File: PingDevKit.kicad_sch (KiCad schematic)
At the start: 54 parts, among them J101 POWER, J102 DEBUG, J103 PORT1, J104 FPGA, J105 ETHERNET, J106 SYNC, J107 SONAR+, J108 SONAR+, J109 SONAR-, J110 SONAR-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

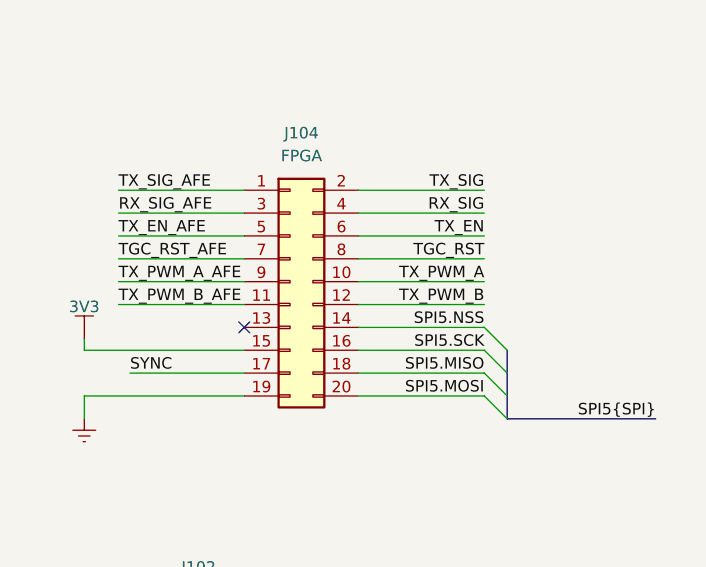
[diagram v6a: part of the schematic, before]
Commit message: new board stackup + routing
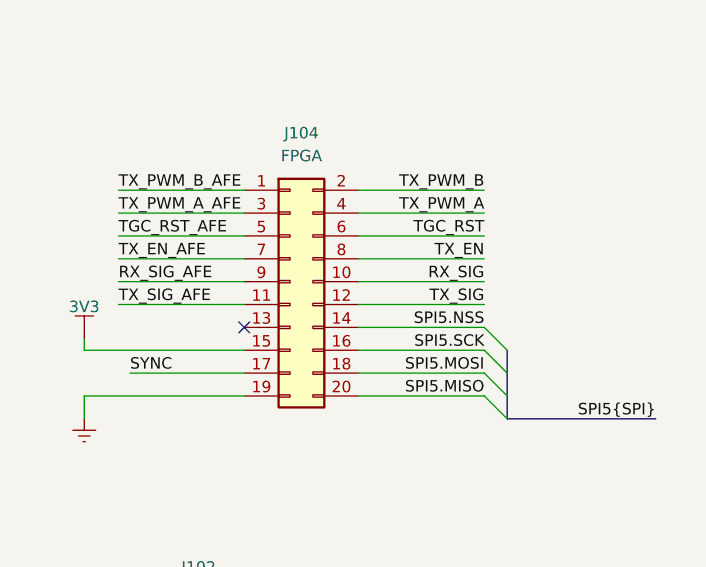
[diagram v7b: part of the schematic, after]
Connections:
- net RX_SIG: now also J104.10 (Pin_10); no longer J104.4 (Pin_4)
- net RX_SIG_AFE: now also J104.9 (Pin_9); no longer J104.3 (Pin_3)
- net SPI5.MISO: now also J104.20 (Pin_20); no longer J104.18 (Pin_18)
- net SPI5.MOSI: now also J104.18 (Pin_18); no longer J104.20 (Pin_20)
- net TGC_RST: now also J104.6 (Pin_6); no longer J104.8 (Pin_8)
- net TGC_RST_AFE: now also J104.5 (Pin_5); no longer J104.7 (Pin_7)
- net TX_EN: now also J104.8 (Pin_8); no longer J104.6 (Pin_6)
- net TX_EN_AFE: now also J104.7 (Pin_7); no longer J104.5 (Pin_5)
- net TX_PWM_A: now also J104.4 (Pin_4); no longer J104.10 (Pin_10)
- net TX_PWM_A_AFE: now also J104.3 (Pin_3); no longer J104.9 (Pin_9)
- net TX_PWM_B: now also J104.2 (Pin_2); no longer J104.12 (Pin_12)
- net TX_PWM_B_AFE: now also J104.1 (Pin_1); no longer J104.11 (Pin_11)
- net TX_SIG: now also J104.12 (Pin_12); no longer J104.2 (Pin_2)
- net TX_SIG_AFE: now also J104.11 (Pin_11); no longer J104.1 (Pin_1)
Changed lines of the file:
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@@
+		)
+	)
+	(label "TX_PWM_B_AFE"
+		(at 38.1 138.43 0)
+		(effects
+			(font
+				(size 1.27 1.27)
+			)
+			(justify left bottom)
 		)
 	)
@@
 		)
 	)
+	(label "TX_EN"
+		(at 78.74 146.05 180)
+		(effects
+			(font
+				(size 1.27 1.27)
+			)
+			(justify right bottom)
+		)
+	)
 	(label "TX_PWM_B"
 		(at 361.95 135.89 180)
@@
 		)
 	)
-	(label "TX_EN_AFE"
-		(at 38.1 143.51 0)
-		(effects
-			(font
-				(size 1.27 1.27)
-			)
-			(justify left bottom)
+	(label "TX_PWM_A"
+		(at 78.74 140.97 180)
+		(effects
+			(font
+				(size 1.27 1.27)
+			)
+			(justify right bottom)
 		)
 	)
@@
 	)
 	(label "TX_SIG"
+		(at 78.74 151.13 180)
+		(effects
+			(font
+				(size 1.27 1.27)
+			)
+			(justify right bottom)
+		)
+	)
+	(label "TX_SIG"
 		(at 269.24 129.54 0)
 		(effects
@@
 			)
 			(justify right bottom)
+		)
+	)
+	(label "TGC_RST_AFE"
+		(at 38.1 143.51 0)
+		(effects
+			(font
+				(size 1.27 1.27)
+			)
+			(justify left bottom)
 		)
 	)
@@
 		)
 	)
-	(label "TX_EN"
-		(at 78.74 143.51 180)
-		(effects
-			(font
-				(size 1.27 1.27)
-			)
-			(justify right bottom)
-		)
-	)
 	(label "VTHERM"
 		(at 269.24 134.62 0)
@@
 		)
 	)
-	(label "TX_PWM_B"
-		(at 78.74 151.13 180)
-		(effects
-			(font
-				(size 1.27 1.27)
-			)
-			(justify right bottom)
+	(label "TX_PWM_A_AFE"
+		(at 38.1 140.97 0)
+		(effects
+			(font
+				(size 1.27 1.27)
+			)
+			(justify left bottom)
 		)
 	)
@@
 			)
 			(justify right bottom)
-		)
-	)
-	(label "TX_PWM_A"
-		(at 78.74 148.59 180)
-		(effects
-			(font
-				(size 1.27 1.27)
-			)
-			(justify right bottom)
-		)
-	)
-	(label "TX_SIG_AFE"
-		(at 38.1 138.43 0)
-		(effects
-			(font
-				(size 1.27 1.27)
-			)
-			(justify left bottom)
 		)
 	)
@@
 		)
 	)
-	(label "RX_SIG"
-		(at 78.74 140.97 180)
-		(effects
-			(font
-				(size 1.27 1.27)
-			)
-			(justify right bottom)
-		)
-	)
 	(label "SPI5.SCK"
 		(at 78.74 156.21 180)
@@
 		)
 	)
-	(label "RX_SIG_AFE"
-		(at 38.1 140.97 0)
-		(effects
-			(font
-				(size 1.27 1.27)
-			)
-			(justify left bottom)
-		)
-	)
 	(label "SONAR-"
 		(at 227.33 330.2 180)
@@
 		)
 	)
-	(label "TX_SIG"
+	(label "TX_PWM_B"
 		(at 78.74 138.43 180)
 		(effects
@@
 		)
 	)
+	(label "SPI5.MISO"
+		(at 78.74 161.29 180)
+		(effects
+			(font
+				(size 1.27 1.27)
+			)
+			(justify right bottom)
+		)
+	)
 	(label "USART1.RX"
 		(at 55.88 196.85 0)
@@
 		)
 	)
+	(label "SPI5.MOSI"
+		(at 78.74 158.75 180)
+		(effects
+			(font
+				(size 1.27 1.27)
+			)
+			(justify right bottom)
+		)
+	)
 	(label "RX-"
 		(at 176.53 372.11 0)
@@
 		)
 	)
-	(label "TX_PWM_B_AFE"
-		(at 38.1 151.13 0)
-		(effects
-			(font
-				(size 1.27 1.27)
-			)
-			(justify left bottom)
-		)
-	)
 	(label "VCC_MODE"
 		(at 361.95 165.1 180)
@@
 		)
 	)
-	(label "SPI5.MISO"
-		(at 78.74 158.75 180)
-		(effects
-			(font
-				(size 1.27 1.27)
-			)
-			(justify right bottom)
-		)
-	)
 	(label "I2C1.SDA"
 		(at 396.24 109.22 180)
@@
 		)
 	)
+	(label "RX_SIG_AFE"
+		(at 38.1 148.59 0)
+		(effects
+			(font
+				(size 1.27 1.27)
+			)
+			(justify left bottom)
+		)
+	)
 	(label "PHY_nRST"
 		(at 262.89 92.71 180)
@@
 		)
 	)
-	(label "SPI5.MOSI"
-		(at 78.74 161.29 180)
-		(effects
-			(font
-				(size 1.27 1.27)
-			)
-			(justify right bottom)
-		)
-	)
-	(label "TGC_RST"
-		(at 78.74 146.05 180)
-		(effects
-			(font
-				(size 1.27 1.27)
-			)
-			(justify right bottom)
-		)
-	)
 	(label "SPI5.NSS"
 		(at 78.74 153.67 180)
@@
 		)
 	)
-	(label "TX_PWM_A_AFE"
-		(at 38.1 148.59 0)
+	(label "TX_SIG_AFE"
+		(at 38.1 151.13 0)
 		(effects
 			(font
@@
 		)
 	)
+	(label "RX_SIG"
+		(at 78.74 148.59 180)
+		(effects
+			(font
+				(size 1.27 1.27)
+			)
+			(justify right bottom)
+		)
+	)
 	(label "TX-"
 		(at 128.27 330.2 0)
@@
 		)
 	)
+	(label "TGC_RST"
+		(at 78.74 143.51 180)
+		(effects
+			(font
+				(size 1.27 1.27)
+			)
+			(justify right bottom)
+		)
+	)
 	(label "TX+"
 		(at 128.27 297.18 0)
@@
 		)
 	)
-	(label "TGC_RST_AFE"
+	(label "TX_EN_AFE"
 		(at 38.1 146.05 0)
 		(effects

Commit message: preboard review of updates
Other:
- sheet TX ports: added none; removed 3V3
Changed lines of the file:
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@@
 	(wire
 		(pts
-			(xy 167.64 196.85) (xy 167.64 207.01)
-		)
-		(stroke
-			(width 0)
-			(type default)
-		)
-	)
-	(wire
-		(pts
 			(xy 55.88 105.41) (xy 55.88 106.68)
 		)
@@
 	(wire
 		(pts
-			(xy 167.64 207.01) (xy 185.42 207.01)
-		)
-		(stroke
-			(width 0)
-			(type default)
-		)
-	)
-	(wire
-		(pts
 			(xy 227.33 54.61) (xy 238.76 54.61)
 		)
@@
 	(symbol
 		(lib_id "BR_Virtual_Parts:VCC")
-		(at 167.64 196.85 0)
-		(unit 1)
-		(exclude_from_sim no)
-		(in_bom yes)
-		(on_board yes)
-		(dnp no)
-		(property "Reference" "#PWR0154"
-			(at 167.64 200.66 0)
-			(effects
-				(font
-					(size 1.27 1.27)
-				)
-				(hide yes)
-			)
-		)
-		(property "Value" "3V3"
-			(at 167.64 193.294 0)
-			(effects
-				(font
-					(size 1.27 1.27)
-				)
-			)
-		)
-		(property "Footprint" ""
-			(at 167.64 196.85 0)
-			(effects
-				(font
-					(size 1.27 1.27)
-				)
-				(hide yes)
-			)
-		)
-		(property "Datasheet" ""
-			(at 167.64 196.85 0)
-			(effects
-				(font
-					(size 1.27 1.27)
-				)
-				(hide yes)
-			)
-		)
-		(property "Description" "Power symbol creates a global label with name \"VCC\""
-			(at 167.64 196.85 0)
-			(effects
-				(font
-					(size 1.27 1.27)
-				)
-				(hide yes)
-			)
-		)
-		(pin "1"
-		)
-		(instances
-			(project "PingDevKit"
-				(path "/2a5ce3ef-537a-4122-a1be-ef76186bc0d7"
-					(reference "#PWR0154")
-					(unit 1)
-				)
-			)
-		)
-	)
-	(symbol
-		(lib_id "BR_Virtual_Parts:VCC")
 		(at 384.81 45.72 0)
 		(unit 1)
@@
 			)
 		)
-		(pin "3V3" input
-			(at 185.42 207.01 180)
-			(effects
-				(font
-					(size 1.27 1.27)
-				)
-				(justify left)
-			)
-		)
